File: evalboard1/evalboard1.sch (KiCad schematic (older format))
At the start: 37 parts, among them J1 USB_OTG, J10 Conn_01x12_Male, J11 Conn_01x18_Male, J12 Conn_01x15_Male, J13 Conn_01x03_Male, J14 power select, J2 RX, J3 TX, J4 analog, J5 IO, J6 core, J7 Conn_01x09_Male, J8 Conn_01x06_Male, J9 Conn_01x17_Male, SW1 SW_Push, U1 GA144A12, U2 FT234XD-R, U3 LTC3406ES5-1.8, U4 SST25WF080B, Y1 Crystal

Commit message: replace USB micro with USB mini
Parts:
- J1: footprint Connector_USB:USB_Micro-B_Amphenol_10103594-0001LF_Horizontal -> Connector_USB:USB_Mini-B_Lumberg_2486_01_Horizontal
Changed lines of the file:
@@
 F 0 "J1" H 10305 1767 50  0000 C CNN
 F 1 "USB_OTG" H 10305 1676 50  0000 C CNN
-F 2 "Connector_USB:USB_Micro-B_Amphenol_10103594-0001LF_Horizontal" H 10400 1250 50  0001 C CNN
+F 2 "Connector_USB:USB_Mini-B_Lumberg_2486_01_Horizontal" H 10400 1250 50  0001 C CNN
 F 3 " ~" H 10400 1250 50  0001 C CNN
 	1    10250 1300

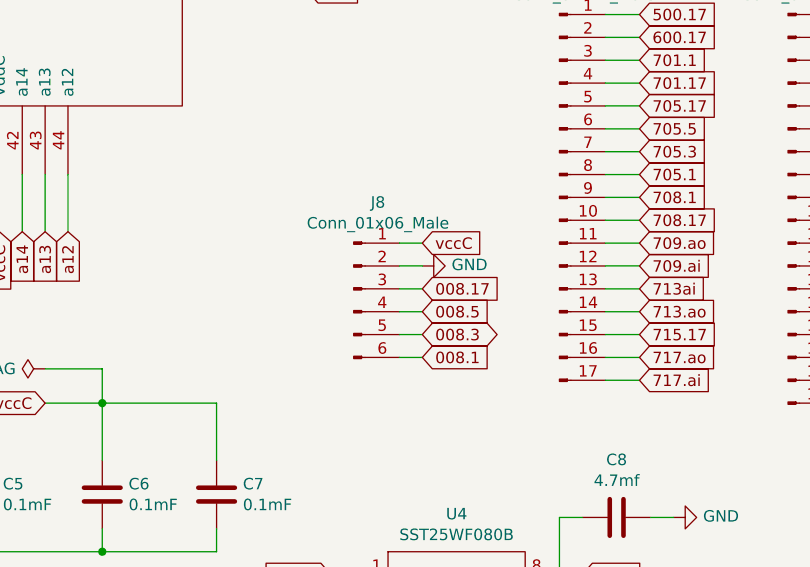
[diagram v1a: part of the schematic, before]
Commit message: evalboard1: add 5v pin to add-on board header
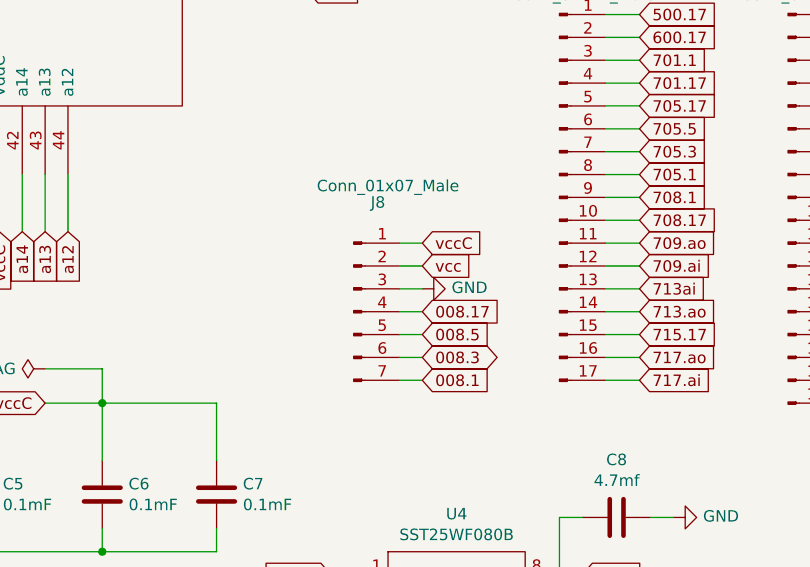
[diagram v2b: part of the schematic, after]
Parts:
- removed J8: Conn_01x06_Male, Connector_PinHeader_2.54mm:PinHeader_1x06_P2.54mm_Vertical, symbol Connector:Conn_01x06_Male
- added J8: Conn_01x07_Male, Connector_PinHeader_2.54mm:PinHeader_1x07_P2.54mm_Vertical, symbol Connector:Conn_01x07_Male
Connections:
- net 008.1: now also J8.7 (Pin_7)
- net 008.17: now also J8.4 (Pin_4)
- net 008.3: now also J8.6 (Pin_6)
- net 008.5: now also J8.5 (Pin_5)
- net GND: now also J8.3 (Pin_3)
- net vcc: now also J8.2 (Pin_2)
- net vccC: now also J8.1 (Pin_1)
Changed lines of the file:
@@
 Text GLabel 7600 5850 2    50   Input ~ 0
 100.17
-Text GLabel 5600 5650 2    50   Input ~ 0
+Text GLabel 5600 5750 2    50   Input ~ 0
 008.17
-Text GLabel 5600 5750 2    50   Input ~ 0
+Text GLabel 5600 5850 2    50   Input ~ 0
 008.5
-Text GLabel 5600 5850 2    50   BiDi ~ 0
+Text GLabel 5600 5950 2    50   BiDi ~ 0
 008.3
-Text GLabel 5600 5950 2    50   Input ~ 0
+Text GLabel 5600 6050 2    50   Input ~ 0
 008.1
 Text GLabel 5600 5450 2    50   Input ~ 0
@@
 L power:GND #PWR05
 U 1 1 5C523692
-P 5600 5550
-F 0 "#PWR05" H 5600 5300 50  0001 C CNN
-F 1 "GND" V 5605 5422 50  0000 R CNN
-F 2 "" H 5600 5550 50  0001 C CNN
-F 3 "" H 5600 5550 50  0001 C CNN
-	1    5600 5550
+P 5600 5650
+F 0 "#PWR05" H 5600 5400 50  0001 C CNN
+F 1 "GND" V 5605 5522 50  0000 R CNN
+F 2 "" H 5600 5650 50  0001 C CNN
+F 3 "" H 5600 5650 50  0001 C CNN
+	1    5600 5650
 	0    -1   -1   0
 $EndComp
@@
 Wire Wire Line
 	8550 4950 8750 4950
-$Comp
-L Connector:Conn_01x06_Male J8
-U 1 1 5C6C1C0B
-P 5300 5650
-F 0 "J8" H 5406 6028 50  0000 C CNN
-F 1 "Conn_01x06_Male" H 5406 5937 50  0000 C CNN
-F 2 "Connector_PinHeader_2.54mm:PinHeader_1x06_P2.54mm_Vertical" H 5300 5650 50  0001 C CNN
-F 3 "~" H 5300 5650 50  0001 C CNN
-	1    5300 5650
-	1    0    0    -1
-$EndComp
 Wire Wire Line
 	5500 5450 5600 5450
 Wire Wire Line
-	5500 5550 5600 5550
-Wire Wire Line
 	5500 5650 5600 5650
 Wire Wire Line
@@
 Wire Wire Line
 	5500 5950 5600 5950
+Wire Wire Line
+	5500 6050 5600 6050
 Wire Wire Line
 	3600 7000 3600 6800
@@
 Wire Wire Line
 	6400 2200 6100 2200
+$Comp
+L Connector:Conn_01x07_Male J8
+U 1 1 5C2A5341
+P 5300 5750
+F 0 "J8" H 5406 6228 50  0000 C CNN
+F 1 "Conn_01x07_Male" H 5450 6300 50  0000 C CNN
+F 2 "Connector_PinHeader_2.54mm:PinHeader_1x07_P2.54mm_Vertical" H 5300 5750 50  0001 C CNN
+F 3 "~" H 5300 5750 50  0001 C CNN
+	1    5300 5750
+	1    0    0    -1
+$EndComp
+Text GLabel 5600 5550 2    50   Input ~ 0
+vcc
+Wire Wire Line
+	5500 5550 5600 5550
 $EndSCHEMATC

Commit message: update library paths
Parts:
- U1: footprint ak-ga144:QFN88+1_GA144A12 -> greenarrays:GA144-QFN88; symbol ak-ga144:GA144A12 -> evalboard1-rescue:GA144A12-ak-ga144
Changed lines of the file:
@@
 $EndDescr
 $Comp
-L ak-ga144:GA144A12 U1
+L evalboard1-rescue:GA144A12-ak-ga144 U1
 U 1 1 5BE088A7
 P 3000 3300
 F 0 "U1" H 2850 3500 50  0000 L CNN
 F 1 "GA144A12" H 2900 3400 50  0000 L CNN
-F 2 "ak-ga144:QFN88+1_GA144A12" H 2750 3350 50  0000 L CNN
+F 2 "greenarrays:GA144-QFN88" H 2750 3350 50  0000 L CNN
 F 3 "" H 3000 3300 50  0001 C CNN
 F 4 "(c) 2014 by Aaron Kondziela" H 3000 5650 60  0001 C BNN "Copyright"
